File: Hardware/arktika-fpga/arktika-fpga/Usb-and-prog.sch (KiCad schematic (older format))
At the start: 17 parts

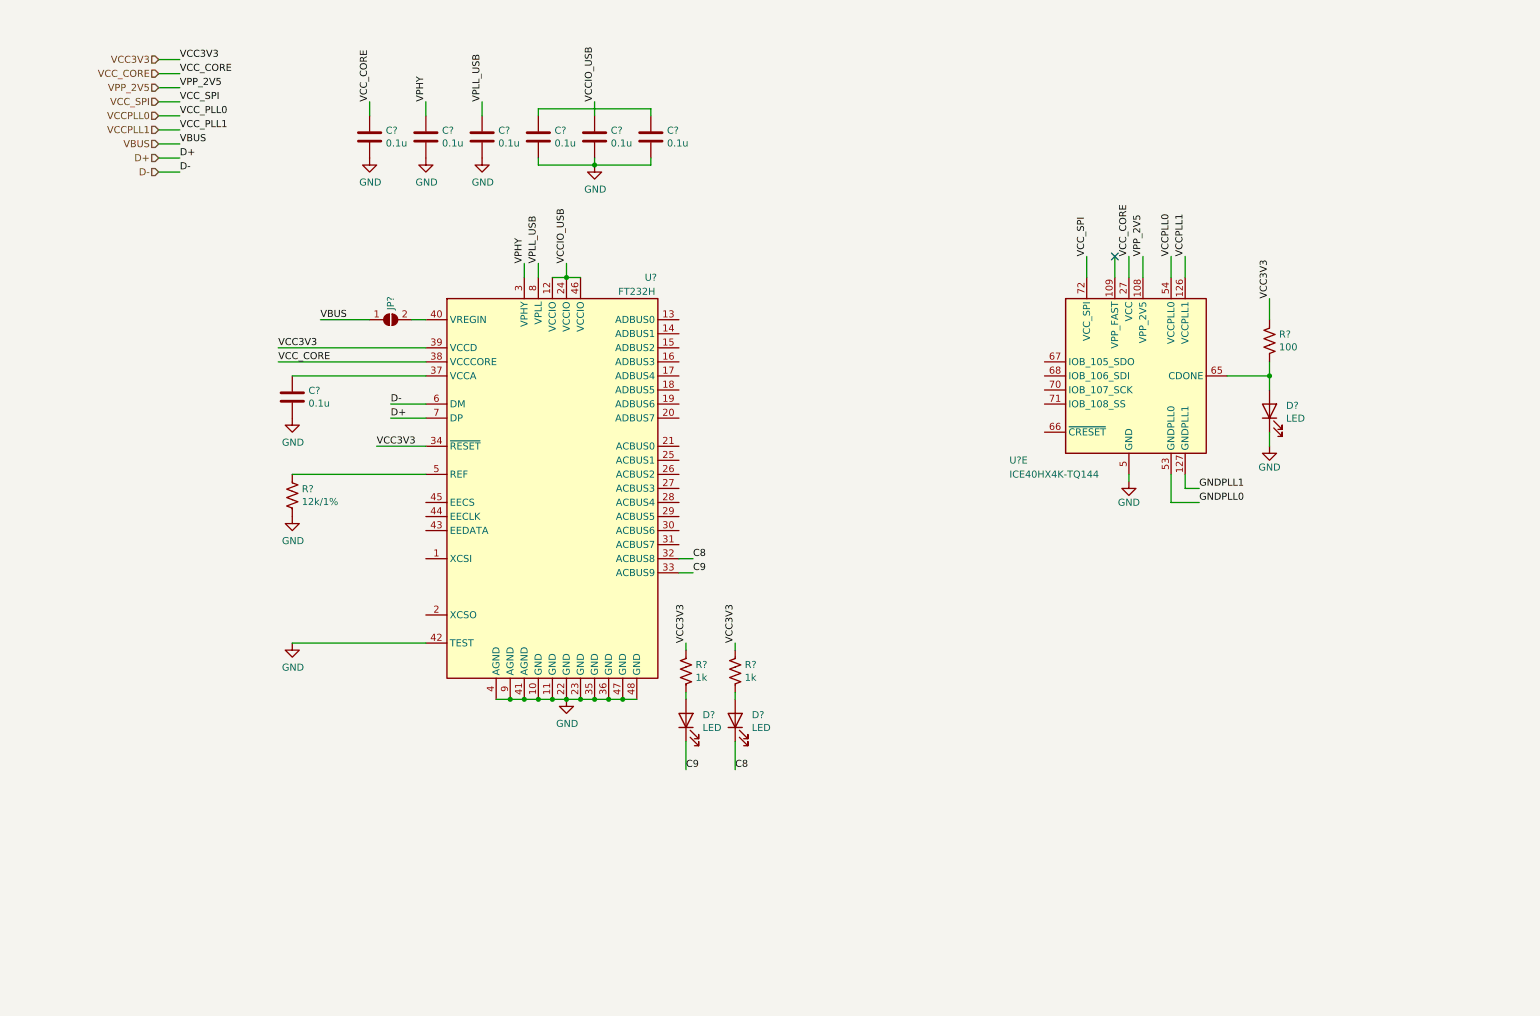
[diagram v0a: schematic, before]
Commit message: Added configuration for power regulation and programming nets
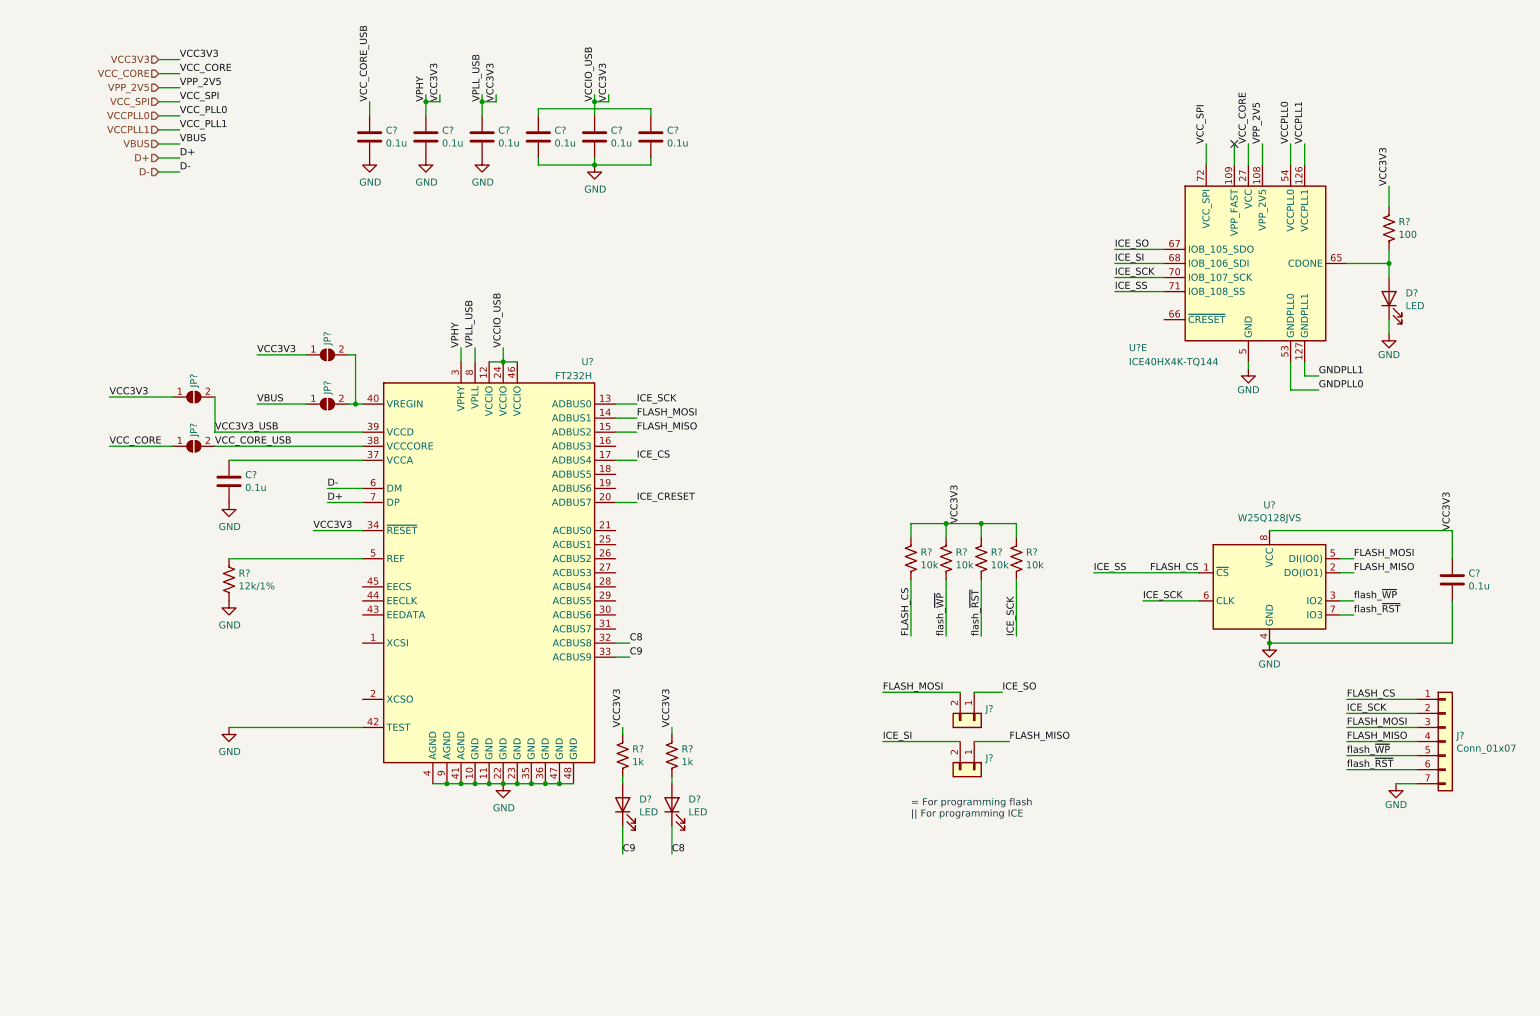
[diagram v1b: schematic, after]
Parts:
- added C?: 0.1u, symbol Device:C
- added J? (x2): Conn_01x02, symbol Connector_Generic:Conn_01x02
- added J?: Conn_01x07, symbol Connector_Generic:Conn_01x07
- added JP? (x3): SolderJumper_2_Open, symbol Jumper:SolderJumper_2_Open
- added R? (x4): 10k, symbol Device:R_US
- added U?: W25Q128JVS, Package_SO:SOIC-8_5.23x5.23mm_P1.27mm, symbol Memory_Flash:W25Q128JVS
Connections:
- net labels added: FLASH_CS, FLASH_MISO, FLASH_MOSI, ICE_CRESET, ICE_CS, ICE_SCK, ICE_SI, ICE_SO, ICE_SS, VCC3V3_USB, VCC_CORE_USB, flash_~RST, flash_~WP
- wire segments 70 -> 127
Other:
- note added: "= For programming flash\n|| For programming ICE\n"
- moved on the sheet: C?, D?, JP?, R?, U?, U?E

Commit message: Added misc components to the usb and prog schematic
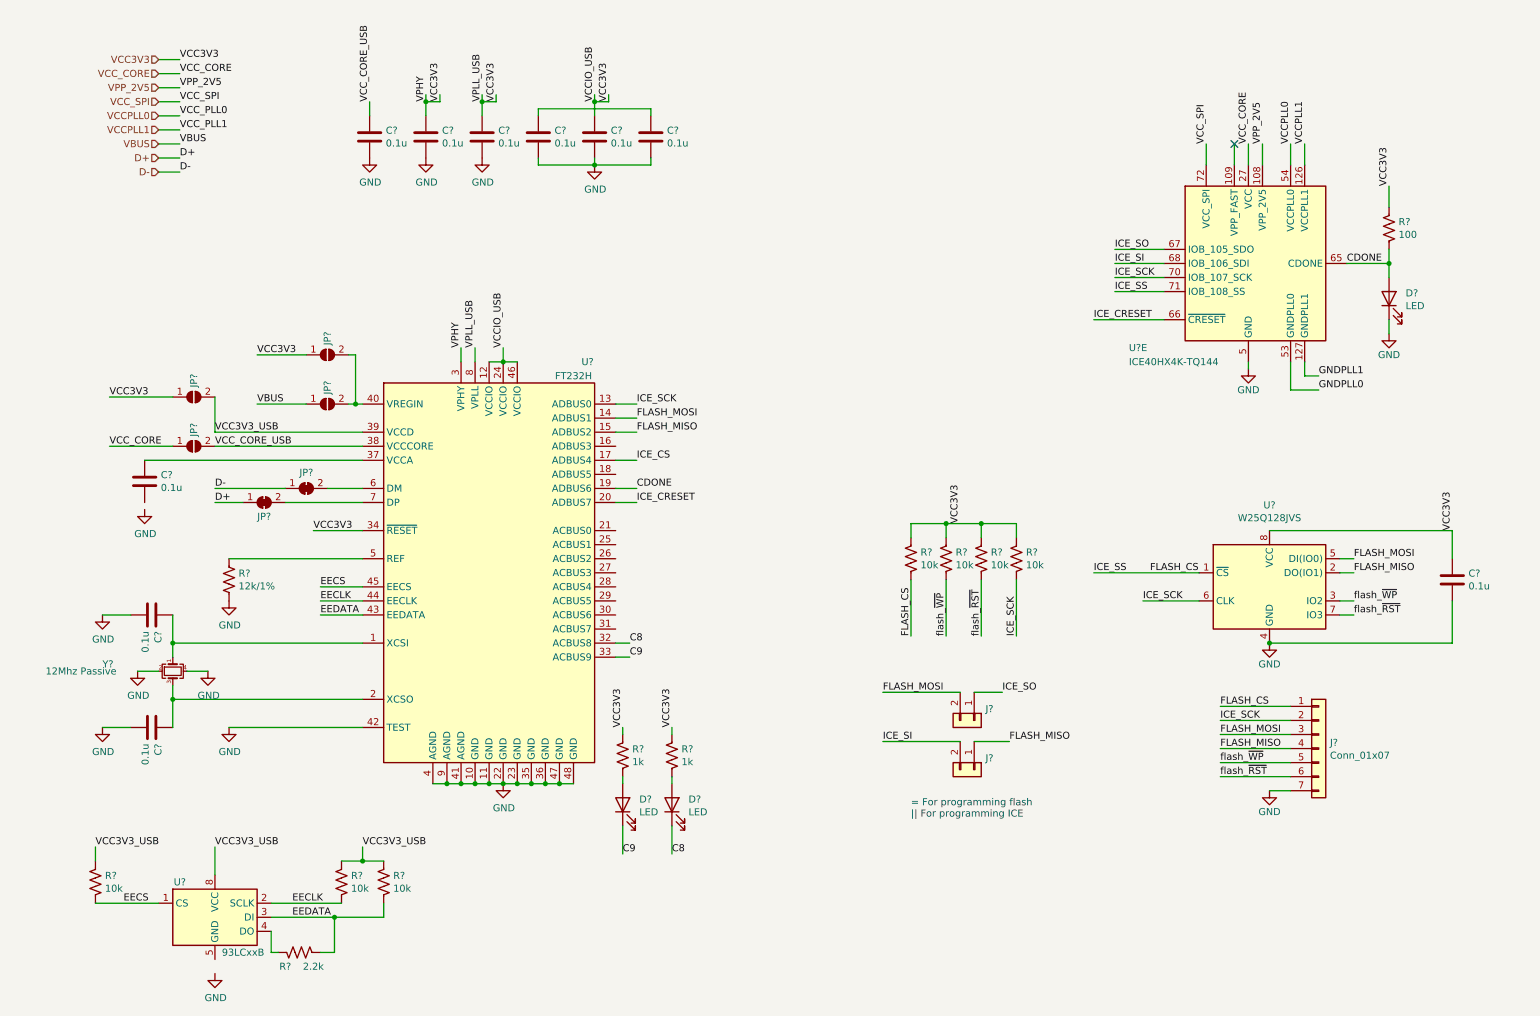
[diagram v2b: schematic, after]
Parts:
- added C? (x2): 0.1u, symbol Device:C
- added JP? (x2): SolderJumper_2_Bridged, symbol Jumper:SolderJumper_2_Bridged
- added R?: 2.2k, symbol Device:R_US
- added R? (x3): 10k, symbol Device:R_US
- added U?: 93LCxxB, symbol Memory_EEPROM:93LCxxB
- added Y?: 12Mhz Passive, Crystals:Crystal_SMD_3225-4pin_3.2x2.5mm_HandSoldering, symbol Device:Crystal_GND24_Small
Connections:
- net labels added: CDONE, EECLK, EECS, EEDATA
- wire segments 127 -> 158
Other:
- moved on the sheet: C?, J?

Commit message: Added designators, some io, and some peripherals
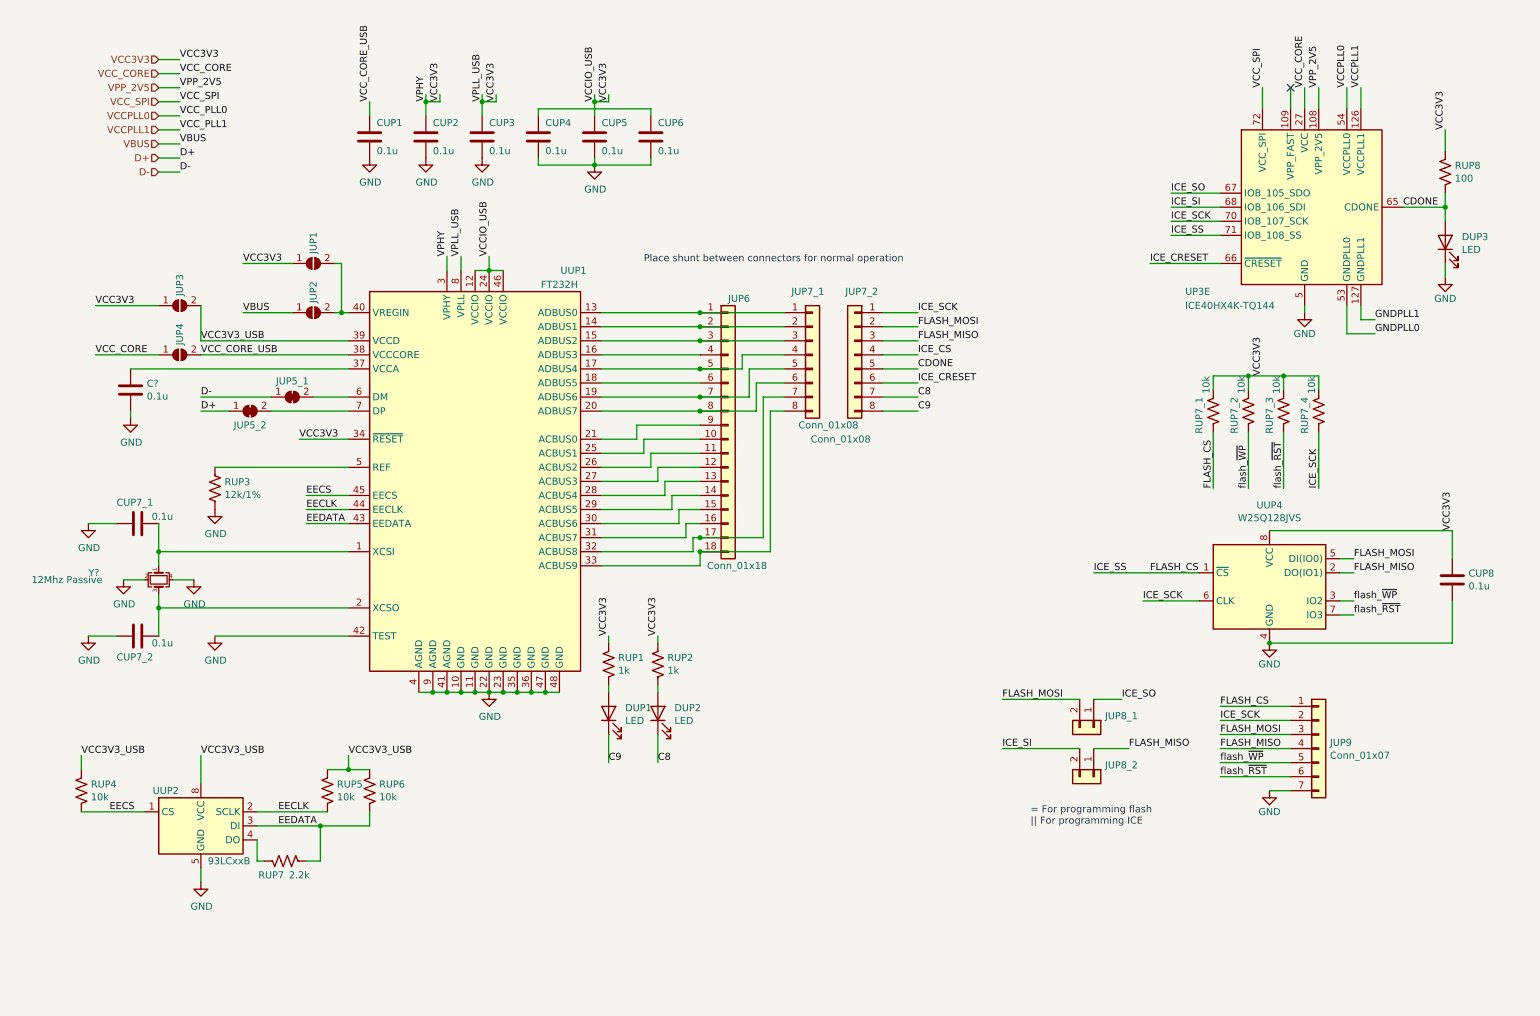
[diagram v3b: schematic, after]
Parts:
- added JUP6: Conn_01x18, symbol Connector_Generic:Conn_01x18
- added JUP7_1, JUP7_2: Conn_01x08, symbol Connector_Generic:Conn_01x08
- gave numbers to parts that had none: 37
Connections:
- wire segments 158 -> 215
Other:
- note added: "Place shunt between connectors for normal operation\n"
- moved on the sheet: C?, CUP7_1, CUP7_2, DUP1, DUP2, DUP3, JUP1, JUP2, JUP3, JUP4, JUP5_1, JUP5_2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

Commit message: Assigned some footprints to components
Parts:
- CUP1, CUP2, CUP3, CUP4, CUP5, CUP6, CUP7_1, CUP7_2, CUP8: footprint (none) -> Capacitors_SMD:C_0603
- RUP1, RUP2, RUP3, RUP4, RUP5, RUP6, RUP7: footprint (none) -> Resistors_SMD:R_0603
- RUP8: value 100 -> 1k; footprint (none) -> Resistors_SMD:R_0603
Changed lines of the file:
@@
 AR Path="/5F415705/5F448AB1" Ref="RUP8"  Part="1"
 F 0 "RUP8" H 10582 1746 50  0000 R CNN
-F 1 "100" H 10582 1655 50  0000 R CNN
-F 2 "" V 10690 1690 50  0001 C CNN
+F 1 "1k" H 10582 1655 50  0000 R CNN
+F 2 "Resistors_SMD:R_0603" V 10690 1690 50  0001 C CNN
 F 3 "~" H 10650 1700 50  0001 C CNN
 	1    10650 1700
@@
 F 0 "CUP2" H 3450 1550 50  0000 L CNN
 F 1 "0.1u" H 3450 1350 50  0000 L CNN
-F 2 "" H 3438 1300 50  0001 C CNN
+F 2 "Capacitors_SMD:C_0603" H 3438 1300 50  0001 C CNN
 F 3 "~" H 3400 1450 50  0001 C CNN
 	1    3400 1450
@@
 F 0 "CUP3" H 3850 1550 50  0000 L CNN
 F 1 "0.1u" H 3850 1350 50  0000 L CNN
-F 2 "" H 3838 1300 50  0001 C CNN
+F 2 "Capacitors_SMD:C_0603" H 3838 1300 50  0001 C CNN
 F 3 "~" H 3800 1450 50  0001 C CNN
 	1    3800 1450
@@
 F 0 "CUP4" H 4250 1550 50  0000 L CNN
 F 1 "0.1u" H 4250 1350 50  0000 L CNN
-F 2 "" H 4238 1300 50  0001 C CNN
+F 2 "Capacitors_SMD:C_0603" H 4238 1300 50  0001 C CNN
 F 3 "~" H 4200 1450 50  0001 C CNN
 	1    4200 1450
@@
 F 0 "CUP5" H 4650 1550 50  0000 L CNN
 F 1 "0.1u" H 4650 1350 50  0000 L CNN
-F 2 "" H 4638 1300 50  0001 C CNN
+F 2 "Capacitors_SMD:C_0603" H 4638 1300 50  0001 C CNN
 F 3 "~" H 4600 1450 50  0001 C CNN
 	1    4600 1450
@@
 F 0 "CUP6" H 5050 1550 50  0000 L CNN
 F 1 "0.1u" H 5050 1350 50  0000 L CNN
-F 2 "" H 5038 1300 50  0001 C CNN
+F 2 "Capacitors_SMD:C_0603" H 5038 1300 50  0001 C CNN
 F 3 "~" H 5000 1450 50  0001 C CNN
 	1    5000 1450
@@
 F 0 "CUP1" H 3050 1550 50  0000 L CNN
 F 1 "0.1u" H 3050 1350 50  0000 L CNN
-F 2 "" H 3038 1300 50  0001 C CNN
+F 2 "Capacitors_SMD:C_0603" H 3038 1300 50  0001 C CNN
 F 3 "~" H 3000 1450 50  0001 C CNN
 	1    3000 1450
@@
 F 0 "RUP3" H 1968 3996 50  0000 L CNN
 F 1 "12k/1%" H 1968 3905 50  0000 L CNN
-F 2 "" V 1940 3940 50  0001 C CNN
+F 2 "Resistors_SMD:R_0603" V 1940 3940 50  0001 C CNN
 F 3 "~" H 1900 3950 50  0001 C CNN
 	1    1900 3950
@@
 F 0 "RUP1" H 4632 5246 50  0000 R CNN
 F 1 "1k" H 4632 5155 50  0000 R CNN
-F 2 "" V 4740 5190 50  0001 C CNN
+F 2 "Resistors_SMD:R_0603" V 4740 5190 50  0001 C CNN
 F 3 "~" H 4700 5200 50  0001 C CNN
 	1    4700 5200
@@
 F 0 "RUP2" H 4982 5246 50  0000 R CNN
 F 1 "1k" H 4982 5155 50  0000 R CNN
-F 2 "" V 5090 5190 50  0001 C CNN
+F 2 "Resistors_SMD:R_0603" V 5090 5190 50  0001 C CNN
 F 3 "~" H 5050 5200 50  0001 C CNN
 	1    5050 5200
@@
 F 0 "CUP8" H 10815 4646 50  0000 L CNN
 F 1 "0.1u" H 10815 4555 50  0000 L CNN
-F 2 "" H 10738 4450 50  0001 C CNN
+F 2 "Capacitors_SMD:C_0603" H 10738 4450 50  0001 C CNN
 F 3 "~" H 10700 4600 50  0001 C CNN
 	1    10700 4600
@@
 F 0 "CUP7_1" V 1200 4050 50  0000 L CNN
 F 1 "0.1u" V 1300 4300 50  0000 L CNN
-F 2 "" H 1388 4050 50  0001 C CNN
+F 2 "Capacitors_SMD:C_0603" H 1388 4050 50  0001 C CNN
 F 3 "~" H 1350 4200 50  0001 C CNN
 	1    1350 4200
@@
 F 0 "CUP7_2" V 1500 4850 50  0000 L CNN
 F 1 "0.1u" V 1400 5100 50  0000 L CNN
-F 2 "" H 1388 4850 50  0001 C CNN
+F 2 "Capacitors_SMD:C_0603" H 1388 4850 50  0001 C CNN
 F 3 "~" H 1350 5000 50  0001 C CNN
 	1    1350 5000
@@
 F 0 "RUP7" V 2300 6500 50  0000 C CNN
 F 1 "2.2k" V 2300 6700 50  0000 C CNN
-F 2 "" V 2440 6590 50  0001 C CNN
+F 2 "Resistors_SMD:R_0603" V 2440 6590 50  0001 C CNN
 F 3 "~" H 2400 6600 50  0001 C CNN
 	1    2400 6600
@@
 F 0 "RUP5" H 2632 6146 50  0000 R CNN
 F 1 "10k" H 2632 6055 50  0000 R CNN
-F 2 "" V 2740 6090 50  0001 C CNN
+F 2 "Resistors_SMD:R_0603" V 2740 6090 50  0001 C CNN
 F 3 "~" H 2700 6100 50  0001 C CNN
 	1    2700 6100
@@
 F 0 "RUP6" H 2932 6146 50  0000 R CNN
 F 1 "10k" H 2932 6055 50  0000 R CNN
-F 2 "" V 3040 6090 50  0001 C CNN
+F 2 "Resistors_SMD:R_0603" V 3040 6090 50  0001 C CNN
 F 3 "~" H 3000 6100 50  0001 C CNN
 	1    3000 6100
@@
 F 0 "RUP4" H 882 6146 50  0000 R CNN
 F 1 "10k" H 882 6055 50  0000 R CNN
-F 2 "" V 990 6090 50  0001 C CNN
+F 2 "Resistors_SMD:R_0603" V 990 6090 50  0001 C CNN
 F 3 "~" H 950 6100 50  0001 C CNN
 	1    950  6100

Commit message: Added alternate power intput. Update some designators. Added fpga crystal
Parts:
- gave numbers to parts that had none: 2
- renumbered CUP7_1 to CUP8_1, CUP7_2 to CUP8_2, CUP8 to CUP9
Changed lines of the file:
@@
 	3850 2400 3950 2400
 $Comp
-L Device:C C?
+L Device:C CUP7
 U 1 1 5F47DBB9
 P 1300 3250
-F 0 "C?" H 1415 3296 50  0000 L CNN
+F 0 "CUP7" H 1415 3296 50  0000 L CNN
 F 1 "0.1u" H 1415 3205 50  0000 L CNN
 F 2 "" H 1338 3100 50  0001 C CNN
@@
 $EndComp
 $Comp
-L Device:C CUP8
+L Device:C CUP9
 U 1 1 5F5400D2
 P 10700 4600
-F 0 "CUP8" H 10815 4646 50  0000 L CNN
+F 0 "CUP9" H 10815 4646 50  0000 L CNN
 F 1 "0.1u" H 10815 4555 50  0000 L CNN
 F 2 "Capacitors_SMD:C_0603" H 10738 4450 50  0001 C CNN
@@
 	9550 5500 9050 5500
 $Comp
-L Device:Crystal_GND24_Small Y?
+L Device:Crystal_GND24_Small YUP1
 U 1 1 5F5F092B
 P 1500 4600
-F 0 "Y?" V 1450 4100 50  0000 L CNN
-F 1 "12Mhz Passive" V 1500 4200 50  0000 R CNN
+F 0 "YUP1" V 1450 4100 50  0000 L CNN
+F 1 "12Mhz Passive" V 1500 4300 50  0000 R CNN
 F 2 "Crystals:Crystal_SMD_3225-4pin_3.2x2.5mm_HandSoldering" H 1500 4600 50  0001 C CNN
 F 3 "~" H 1500 4600 50  0001 C CNN
@@
 $EndComp
 $Comp
-L Device:C CUP7_1
+L Device:C CUP8_1
 U 1 1 5F60959E
 P 1350 4200
-F 0 "CUP7_1" V 1200 4050 50  0000 L CNN
+F 0 "CUP8_1" V 1200 4050 50  0000 L CNN
 F 1 "0.1u" V 1300 4300 50  0000 L CNN
 F 2 "Capacitors_SMD:C_0603" H 1388 4050 50  0001 C CNN
@@
 $EndComp
 $Comp
-L Device:C CUP7_2
+L Device:C CUP8_2
 U 1 1 5F609C00
 P 1350 5000
-F 0 "CUP7_2" V 1500 4850 50  0000 L CNN
+F 0 "CUP8_2" V 1500 4850 50  0000 L CNN
 F 1 "0.1u" V 1400 5100 50  0000 L CNN
 F 2 "Capacitors_SMD:C_0603" H 1388 4850 50  0001 C CNN
@@
 	5300 4400 5300 4300
 Wire Wire Line
-	5300 4300 5350 4300
-Wire Wire Line
 	4650 4400 5300 4400
 Wire Wire Line
@@
 	5350 3400 5750 3400
 Wire Wire Line
-	5350 4300 5800 4300
-Wire Wire Line
 	5800 4300 5800 3300
 Wire Wire Line
 	5800 3300 5950 3300
-Connection ~ 5350 4300
 Wire Wire Line
 	5350 4400 5850 4400
@@
 Wire Wire Line
 	1300 3400 1300 3450
+Wire Wire Line
+	5300 4300 5350 4300
+Connection ~ 5350 4300
+Wire Wire Line
+	5350 4300 5800 4300
 $EndSCHEMATC
